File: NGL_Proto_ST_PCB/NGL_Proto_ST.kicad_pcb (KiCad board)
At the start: 2 copper layers, 113 x 70 mm, 130 parts, among them J1 Conn_01x08_Male, J2 Conn_01x04_Male, J3 227161-2, J4 Conn_01x06_Male, J5 Conn_01x04_Male, J6 Conn_01x03_Male, SW3 SW_Push, SW4 SW_Push, U1 AD8639, U2 AD8639, U3 MAX922CSAT, U4 ESP32-WROOM-32D-N16, U5 LF33CDT-TR, U6 MAX860ESA+T, U7 AD620, U8 AD8639, U9 MCP3426A0-E_SN

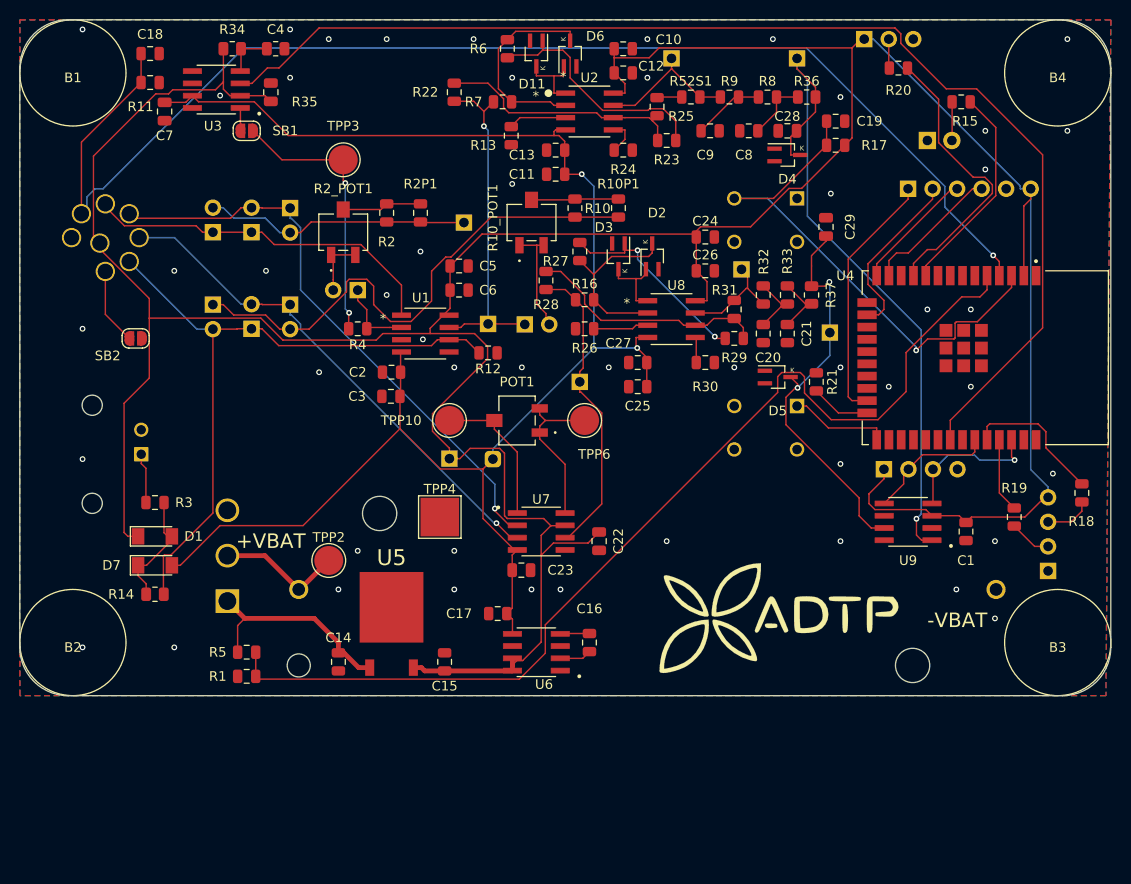
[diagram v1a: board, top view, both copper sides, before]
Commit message: Ajuut nouveaux composants: commande 3
Attente question ENABL E + POTAR
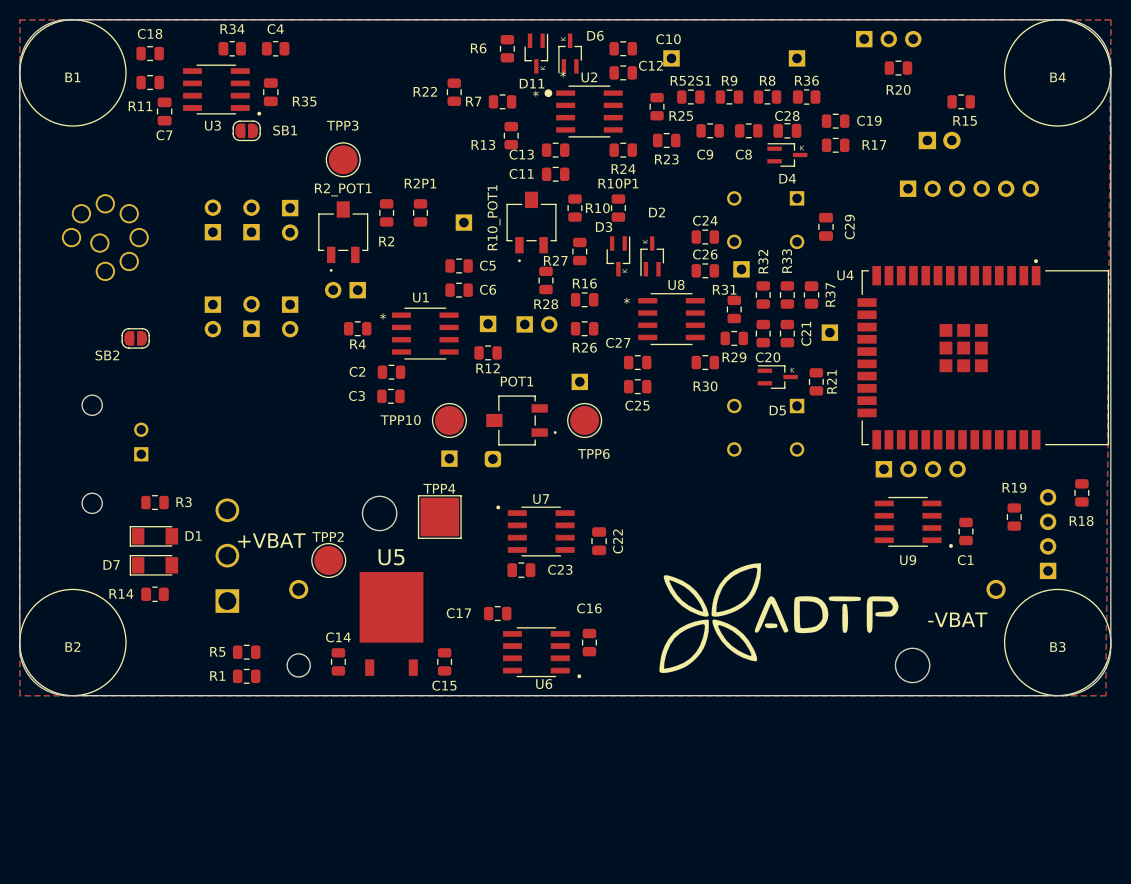
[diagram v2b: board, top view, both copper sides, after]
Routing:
- net +3V3: track 373.3 -> 0.00 mm
- net -3V3: track 164.8 -> 0.00 mm, vias 2 -> 0
- net OUT_NTC: track 134.0 -> 0.00 mm, vias 1 -> 0
- net CLOCK_GEN: track 125.0 -> 0.00 mm
- net OUT_BAT: track 106.6 -> 0.00 mm
- net CURRENT_3: track 70.7 -> 0.00 mm
- net OUT_SENS: track 69.6 -> 0.00 mm, vias 1 -> 0
- net DIFF-: track 60.5 -> 0.00 mm, vias 1 -> 0
- net Net-(JP8-Pad1): track 55.0 -> 0.00 mm
- net /ESP32/EN: track 54.6 -> 0.00 mm, vias 1 -> 0
- net DIFF+: track 53.0 -> 0.00 mm, vias 1 -> 0
- net OUT_DIFF: track 41.8 -> 0.00 mm, vias 2 -> 0
- net CURRENT_4: track 37.4 -> 0.00 mm
- net Net-(JP3-Pad1): track 34.7 -> 0.00 mm, vias 1 -> 0
- net /Ampli Diff/620: track 31.4 -> 0.00 mm
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
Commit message: Avancement après réunion mercredi
finir pour mettre en review puis attente.
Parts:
- added C30: 1uF, Capacitor_SMD:C_0805_2012Metric, F.Cu at (144.3, 133.8)
- added M1: ROB-08449, Connector_PinHeader_2.54mm:PinHeader_1x02_P2.54mm_Vertical, F.Cu at (177.5, 130.3)
- added R38: RU1C002UNTCL, Lib_NGL_ST:RU1C002UNTCL, F.Cu at (173.0, 133.5)
- added R39: 0R, Resistor_SMD:R_0805_2012Metric, F.Cu at (144.3, 136.7)
- added U10: 10K, Lib_NGL_ST:max5481eud&plus_T, F.Cu at (125.0, 125.5)
- added U11: 20k, Lib_NGL_ST:SOP50P490X110-10N, F.Cu at (111.0, 123.5)
- U5: value LF33CDT-TR -> LD29080PT33R; footprint Lib_NGL_Proto:TO228P972X240-3N -> Lib_NGL_ST:DPAK114P990X239-6N
- moved U5 25.5 mm to (153.0, 132.0)
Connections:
- C15 pad 1: +3V3 -> Net-(C15-Pad1)
- TP7 pad 1: +3V3 -> Net-(TP7-Pad1)
- U3 pad 2: +3V3 -> -3V3
- U3 pad 7: -3V3 -> +3V3
- U4 pad 23: CS -> Net-(U4-Pad23)
- U4 pad 27: Net-(U4-Pad27) -> CS_R10
- U4 pad 28: Net-(U4-Pad28) -> CS_R2
- U4 pad 30: Net-(U4-Pad30) -> MOTEUR
- U5 pad 1: +BATT -> ENABLE
- U5 pad 2: -BATT -> +BATT
- U5 pad 3: +3V3 -> Net-(U5-Pad3)

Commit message: Commit avant DSN
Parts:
- removed R10_POT1, R2_POT1: R2_POT, Lib_NGL_Proto:3224X-1-502E
- added C31: 100nF, Capacitor_SMD:C_0805_2012Metric_Pad1.18x1.45mm_HandSolder, F.Cu at (134.0, 53.0)
- added C32: 100nF, Capacitor_SMD:C_0805_2012Metric_Pad1.18x1.45mm_HandSolder, F.Cu at (150.0, 66.5)
- added SB3: SB, Jumper:SolderJumper-2_P1.3mm_Open_RoundedPad1.0x1.5mm, F.Cu at (150.0, 78.0)
- added SB4: SB, Jumper:SolderJumper-2_P1.3mm_Open_RoundedPad1.0x1.5mm, F.Cu at (133.5, 86.0)
- C1, C10, C11, C12, C13, C14, C15, C17, C18, C19, C2, C20, C21, C22, C23, C24, C25, C26, C27, C28, C29, C3, C30, C4, C5, C6, C7, C8, C9: footprint Capacitor_SMD:C_0805_2012Metric -> Capacitor_SMD:C_0805_2012Metric_Pad1.18x1.45mm_HandSolder
- C16: value 10uF -> 4.7uF; footprint Capacitor_SMD:C_0805_2012Metric -> Capacitor_SMD:C_0805_2012Metric_Pad1.18x1.45mm_HandSolder
- R1, R10, R10P1, R11, R12, R13, R14, R15, R16, R17, R2, R20, R21, R22, R23, R24, R25, R26, R27, R28, R29, R2P1, R3, R30, R31, R32, R33, R34, R35, R36, R37, R39, R4, R5, R52S1, R6, R7, R8, R9: footprint Resistor_SMD:R_0805_2012Metric -> Resistor_SMD:R_0805_2012Metric_Pad1.20x1.40mm_HandSolder
- U6: value MAX860ESA+T -> MAX1680ESA+T; footprint Lib_NGL_Proto:SOIC127P600X175-8N -> Lib_NGL_ST:SOIC127P600X175-8N
- moved R39 83.8 mm to (140.0, 53.0)
- moved U10 67.9 mm to (136.0, 58.5)
- moved C30 67.3 mm to (145.5, 66.5)
- moved U11 66.3 mm to (151.5, 71.0)
- moved M1 26.1 mm to (198.2, 114.5)
- moved U5 24.4 mm to (139.0, 112.0)
- moved T1 19.8 mm to (183.9, 117.0), turned to 270 degrees
- moved TPP3 5.39 mm to (128.5, 62.5)
- moved SB2 4.14 mm to (109.2, 80.0)
- moved C14 2.76 mm to (132.3, 113.8)
- moved U6 0.50 mm to (153.5, 116.0), turned to 0 degrees
- renumbered R38 to T1
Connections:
- BT1 pad P: Net-(BT1-PadP) -> +BATT
- C15 pad 1: Net-(C15-Pad1) -> +3V3
- J2 pad 2: Net-(J2-Pad2) -> UART_TX
- J2 pad 3: Net-(J2-Pad3) -> UART_RX
- J4 pad 1: CS -> CS_R2
- R10 pad 2: Net-(R10-Pad2) -> R10_IN
- R10P1 pad 2: Net-(R10-Pad2) -> R10_IN
- R2 pad 2: Net-(R2-Pad2) -> R2_IN
- R22 pad 1: Net-(JP3-Pad1) -> R10_OUT
- R2P1 pad 2: Net-(R2-Pad2) -> R2_IN
- R4 pad 1: Net-(JP11-Pad1) -> R2_OUT
- R7 pad 1: Net-(JP3-Pad1) -> R10_OUT
- S1 pad 1: +BATT -> OUT_BAT
- S1 pad 2: Net-(BT1-PadP) -> INH
- TP3 pad 1: Net-(JP3-Pad1) -> R10_OUT
- TP7 pad 1: Net-(TP7-Pad1) -> +3V3
- TPP2 pad 1: Net-(BT1-PadP) -> +BATT
- U1 pad 2: Net-(JP11-Pad1) -> R2_OUT
- U1 pad 7: Net-(JP3-Pad1) -> R10_OUT
- U4 pad 37: Net-(U4-Pad37) -> INH
- U5 pad 1: ENABLE -> INH
- U5 pad 3: Net-(U5-Pad3) -> -BATT
- U5 pad 4: Net-(U5-Pad4) -> +3V3
- U6 pad 1: -BATT -> +3V3
- U6 pad 7: +3V3 -> -BATT
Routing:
- net -3V3: track 0.00 -> 191.2 mm, vias 0 -> 5
- net +BATT: track 0.00 -> 18.7 mm
- net +3V3: track 0.00 -> 7.04 mm
- net INH: track 0.00 -> 1.00 mm
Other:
- board text added: "+"

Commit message: essai pas mal
commit avant review
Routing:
- net +3V3: track 7.04 -> 434.9 mm, vias 0 -> 1
- net OUT_NTC: track 0.00 -> 131.9 mm
- net CLOCK_GEN: track 0.00 -> 120.4 mm
- net INH: track 1.00 -> 118.2 mm
- net OUT_BAT: track 0.00 -> 107.0 mm, vias 0 -> 1
- net CLK: track 0.00 -> 91.2 mm, vias 0 -> 1
- net CS_R2: track 0.00 -> 90.1 mm, vias 0 -> 1
- net MOSI: track 0.00 -> 82.9 mm
- net CURRENT_3: track 0.00 -> 71.6 mm, vias 0 -> 1
- net OUT_SENS: track 0.00 -> 71.6 mm, vias 0 -> 1
- net DIFF-: track 0.00 -> 63.6 mm, vias 0 -> 1
- net DIFF+: track 0.00 -> 53.8 mm
- net CS_R10: track 0.00 -> 53.2 mm, vias 0 -> 2
- net Net-(JP8-Pad1): track 0.00 -> 51.2 mm, vias 0 -> 1
- net R10_OUT: track 0.00 -> 43.6 mm, vias 0 -> 1
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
